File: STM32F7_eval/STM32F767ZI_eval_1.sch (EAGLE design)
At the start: 107 parts, among them CN1 GROVE-4P-CONN-I2C-90D, CN2 GROVE-4P-CONN-I2C-90D, CN3 GROVE-4P-CONN-I2C-90D, CN4 GROVE-4P-CONN-AN01-90D, CN5 ARDUINO_COMPAT_IF, CN6 STLINKV21_SWD_IF, CN7 WFT0750CZ09-SMD_, CN8 MCO_IF, CN9 UART_IF, Q1 PMF370XN_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

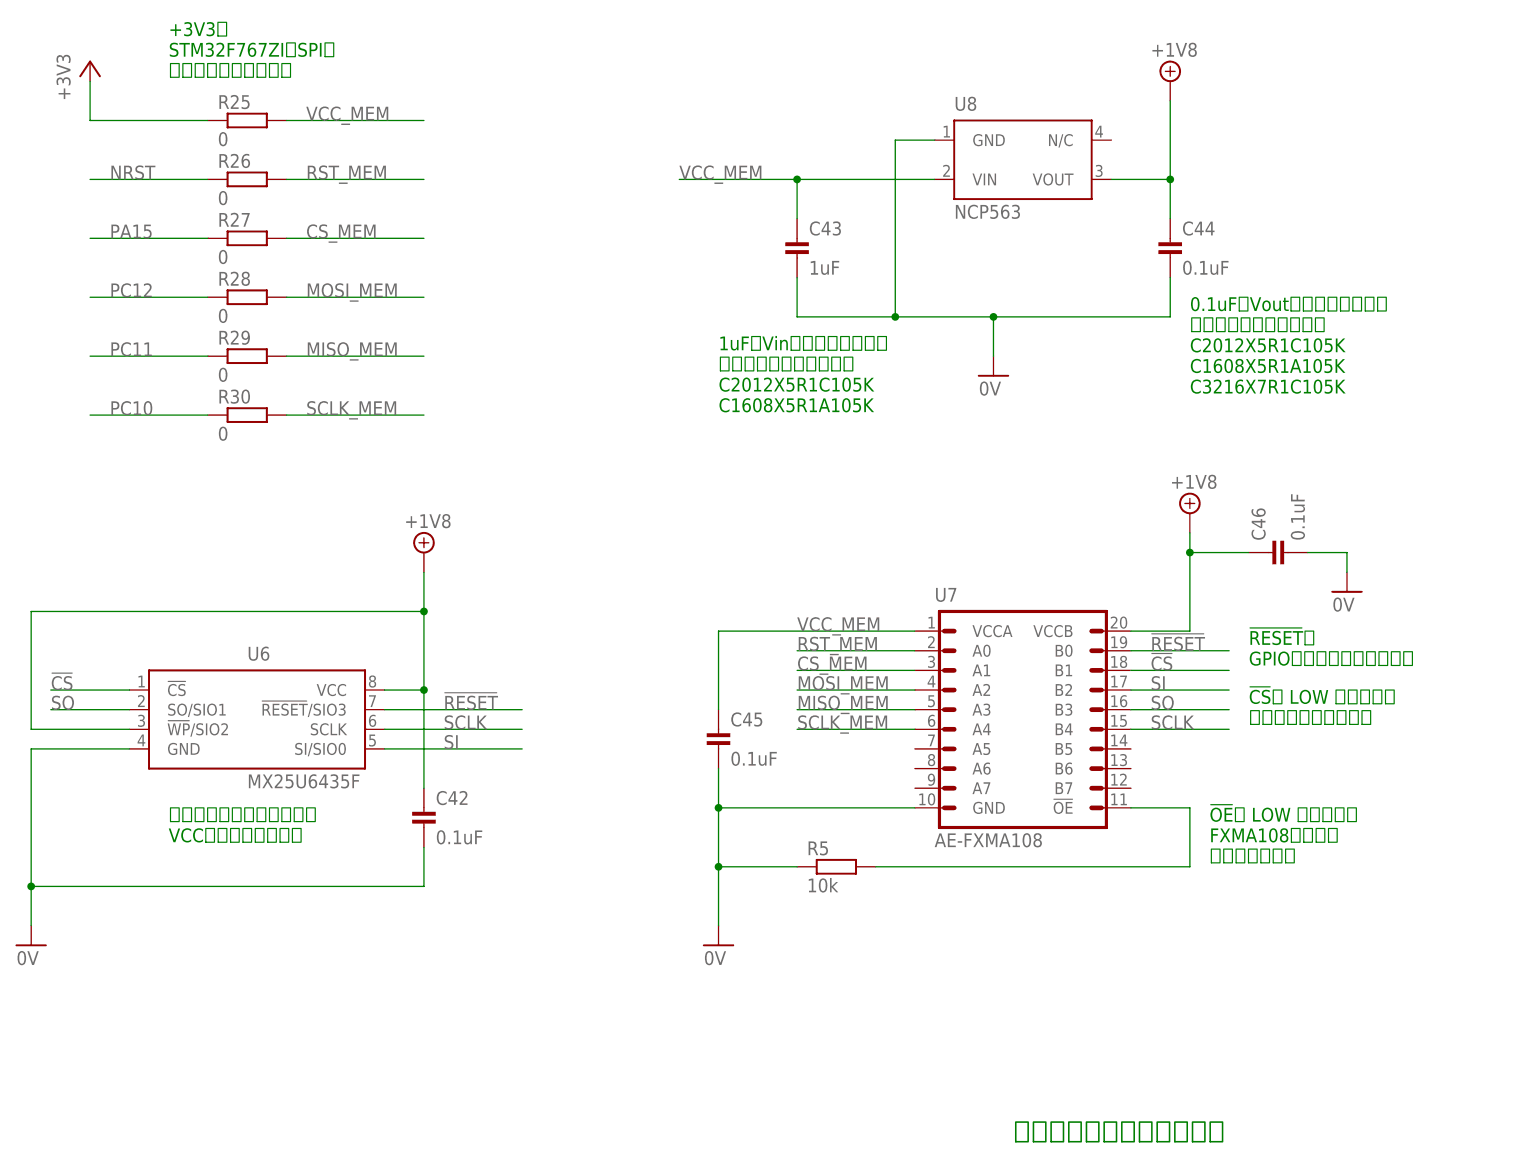
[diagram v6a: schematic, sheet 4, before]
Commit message: 評価回路を修正
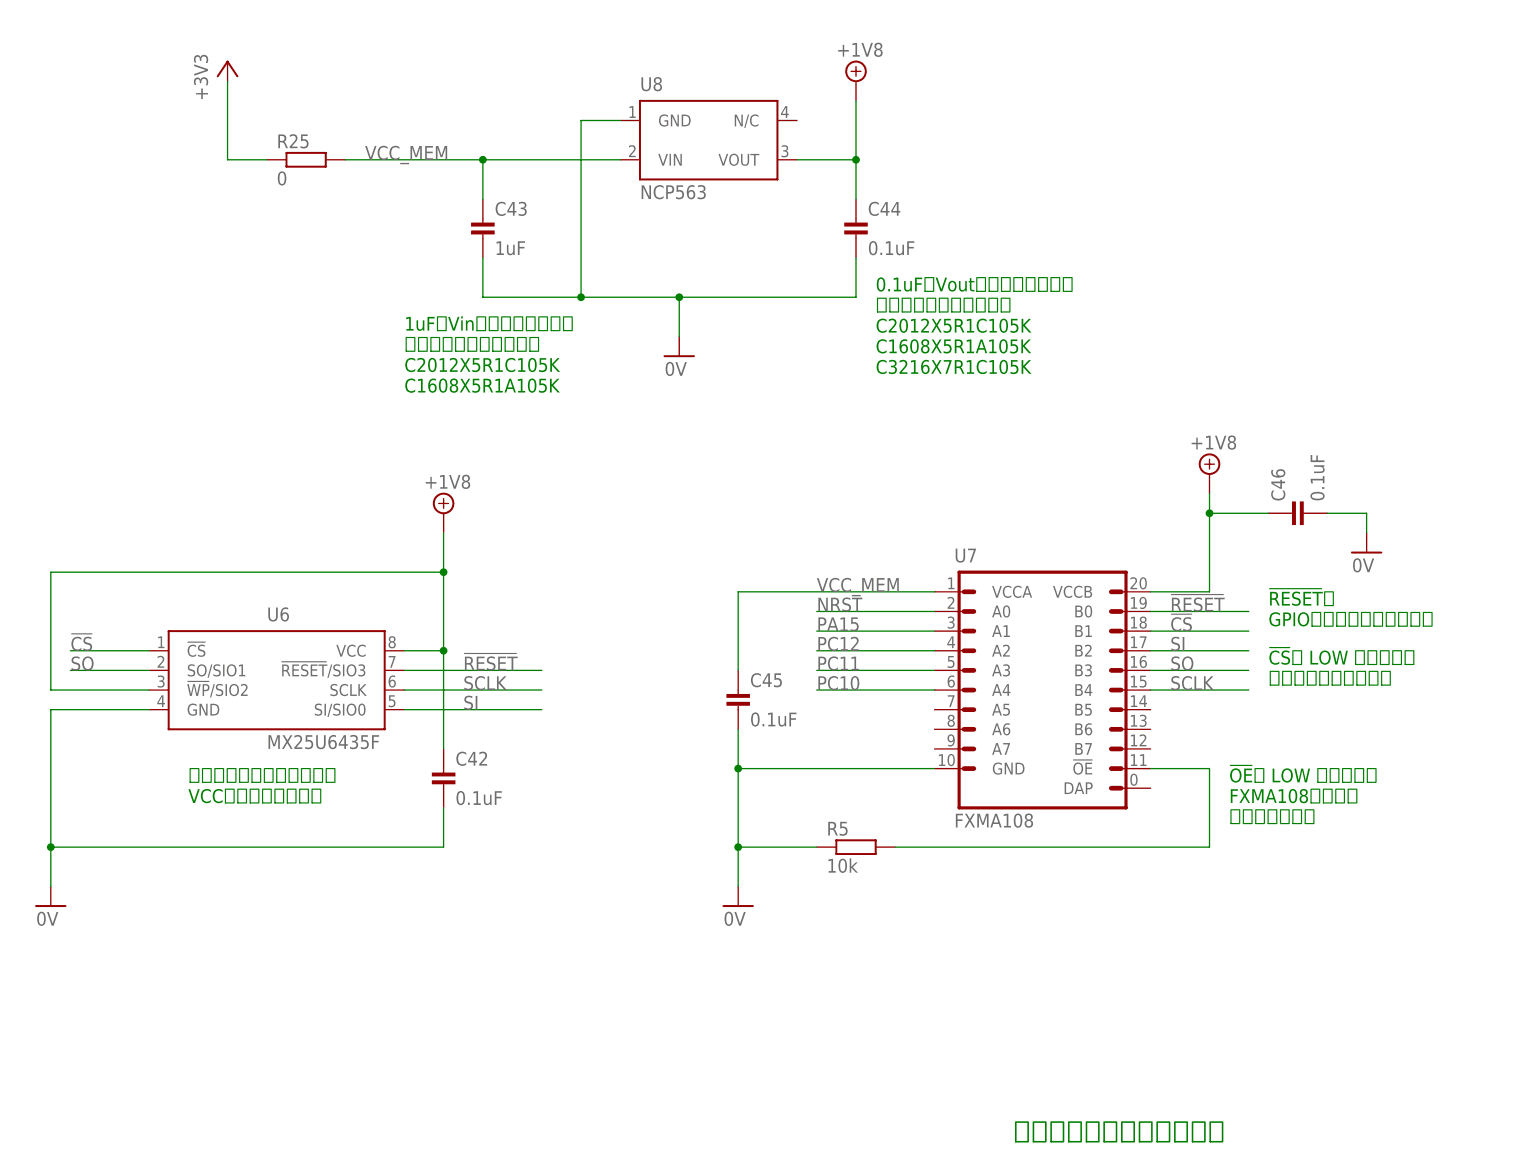
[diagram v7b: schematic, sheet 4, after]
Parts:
- removed CN1, CN2: GROVE-4P-CONN-I2C-90D, PartsForProto:GROVE-4P-CONN-I2C-90D
- removed R26, R27, R28, R29, R30: 0, Parts:RESISTOR_0603_DEV
- U7: value AE-FXMA108 -> FXMA108; device PartsForProto:AE-FXMA108 -> Parts:FXMA108
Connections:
- removed net CS_MEM: R27.2, U7.A1
- removed net MISO_MEM: R29.2, U7.A3
- removed net MOSI_MEM: R28.2, U7.A2
- removed net RST_MEM: R26.2, U7.A0
- removed net SCLK_MEM: R30.2, U7.A4
- net 0V: no longer CN1.GND, CN2.GND
- net NRST: now also U7.A0; no longer R26.1
- net PA15: now also U7.A1; no longer R27.1
- net PB8: no longer CN1.SCL, CN2.SCL
- net PB9: no longer CN1.SDA, CN2.SDA
- net PC10: now also U7.A4; no longer R30.1
- net PC11: now also U7.A3; no longer R29.1
- net PC12: now also U7.A2; no longer R28.1
- net VDD: no longer CN1.VCC, CN2.VCC
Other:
- note added: "Groveコネクター ・I2Cポート ・アナログポート"
- note removed: "+3V3と STM32F767ZIのSPIに ジャンパーを介し接続"
- note removed: "Groveコネクター ・I2C３ポート ・アナログ１ポート"
- moved on the sheet: C42, C43, C44, C45, C46, CN3, CN4, R25, R5, U6, U8
